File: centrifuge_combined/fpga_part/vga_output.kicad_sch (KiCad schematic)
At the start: 15 parts, among them U5 THS8136

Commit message: Fixed missing footprints, added decoupling capacitors, adjusted board edges
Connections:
- net GND: now also U5.49 (THERMAL)
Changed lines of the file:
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@@
     (title "VGA Centrifuge")
     (date "2022-10-03")
-    (rev "R2")
+    (rev "R3")
     (comment 1 "Author: Paolo Celati")
     (comment 2 "VGA DAC")
@@
   (symbol (lib_id "centrifuge_symbols:THS8136") (at 178.435 69.85 180) (unit 1)
     (in_bom yes) (on_board yes) (fields_autoplaced)
-    (property "Reference" "U5" (id 0) (at 146.05 90.3988 0))
-    (property "Value" "THS8136" (id 1) (at 146.05 87.8588 0))
+    (property "Reference" "U5" (id 0) (at 210.82 49.3012 0))
+    (property "Value" "THS8136" (id 1) (at 210.82 51.8412 0))
     (property "Footprint" "Package_QFP:LQFP-48-1EP_7x7mm_P0.5mm_EP3.6x3.6mm" (id 2) (at 178.435 69.85 0)
       (effects (font (size 1.27 1.27)) hide)
@@
       (effects (font (size 1.27 1.27)) hide)
     )
+    (pin "49")
     (pin "1")
     (pin "10")

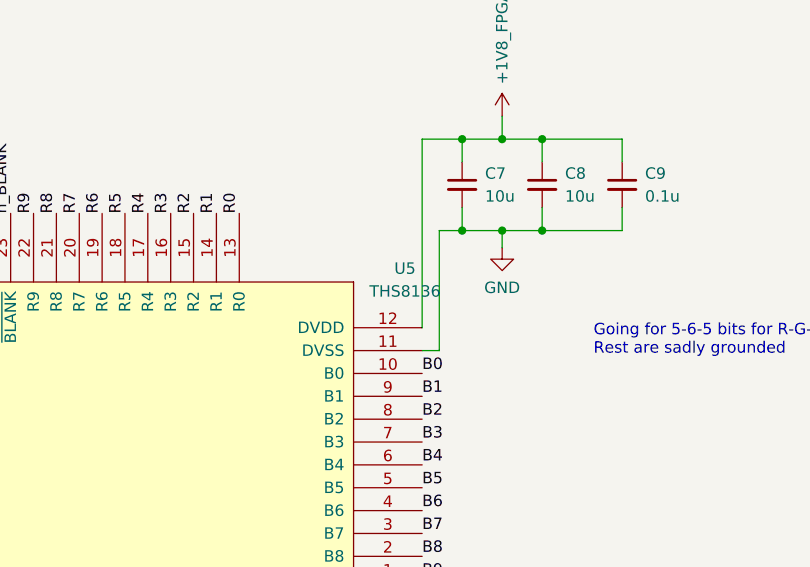
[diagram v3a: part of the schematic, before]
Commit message: Fixed Elprint complaints and JTAG VREF problems+config flash CS
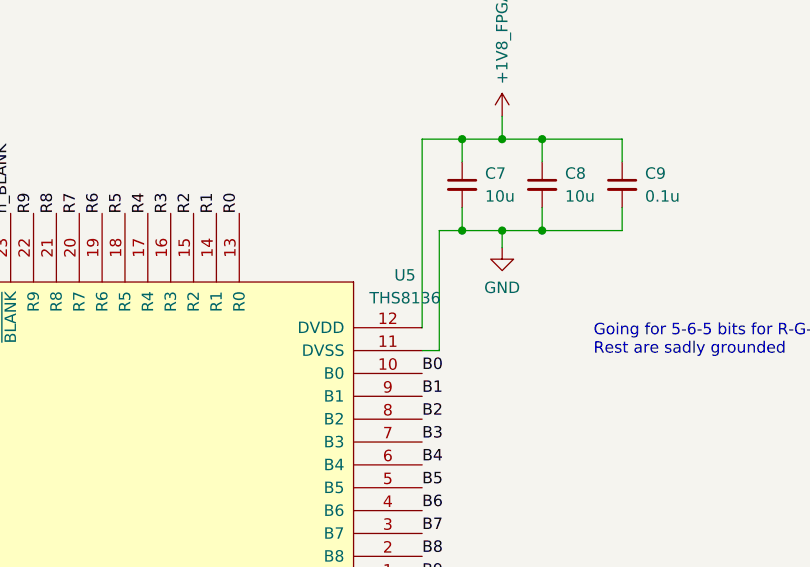
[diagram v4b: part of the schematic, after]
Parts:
- U5: footprint Package_QFP:LQFP-48-1EP_7x7mm_P0.5mm_EP3.6x3.6mm -> centrifuge footprints:LQFP-48-1EP_7x7mm_P0.5mm_EP3.6x3.6mm_ThermalVias_modified
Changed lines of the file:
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@@
   (title_block
     (title "VGA Centrifuge")
-    (date "2022-10-03")
-    (rev "R3")
+    (date "2022-10-05")
+    (rev "R4")
     (comment 1 "Author: Paolo Celati")
     (comment 2 "VGA DAC")
@@
   (symbol (lib_id "centrifuge_symbols:THS8136") (at 178.435 69.85 180) (unit 1)
     (in_bom yes) (on_board yes) (fields_autoplaced)
-    (property "Reference" "U5" (id 0) (at 210.82 49.3012 0))
-    (property "Value" "THS8136" (id 1) (at 210.82 51.8412 0))
-    (property "Footprint" "Package_QFP:LQFP-48-1EP_7x7mm_P0.5mm_EP3.6x3.6mm" (id 2) (at 178.435 69.85 0)
-      (effects (font (size 1.27 1.27)) hide)
-    )
+    (property "Reference" "U5" (id 0) (at 210.82 50.0505 0))
+    (property "Value" "THS8136" (id 1) (at 210.82 52.5905 0))
+    (property "Footprint" "centrifuge footprints:LQFP-48-1EP_7x7mm_P0.5mm_EP3.6x3.6mm_ThermalVias_modified" (id 2) (at 178.435 69.85 0)
+      (effects (font (size 1.27 1.27)) hide)
+    )
